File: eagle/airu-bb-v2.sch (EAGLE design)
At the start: 25 parts, among them Q2 MOSFET-NCHANNELAO3404A, U1 BMP180, U2 DHT22, U3 GPS, X2 53261-08

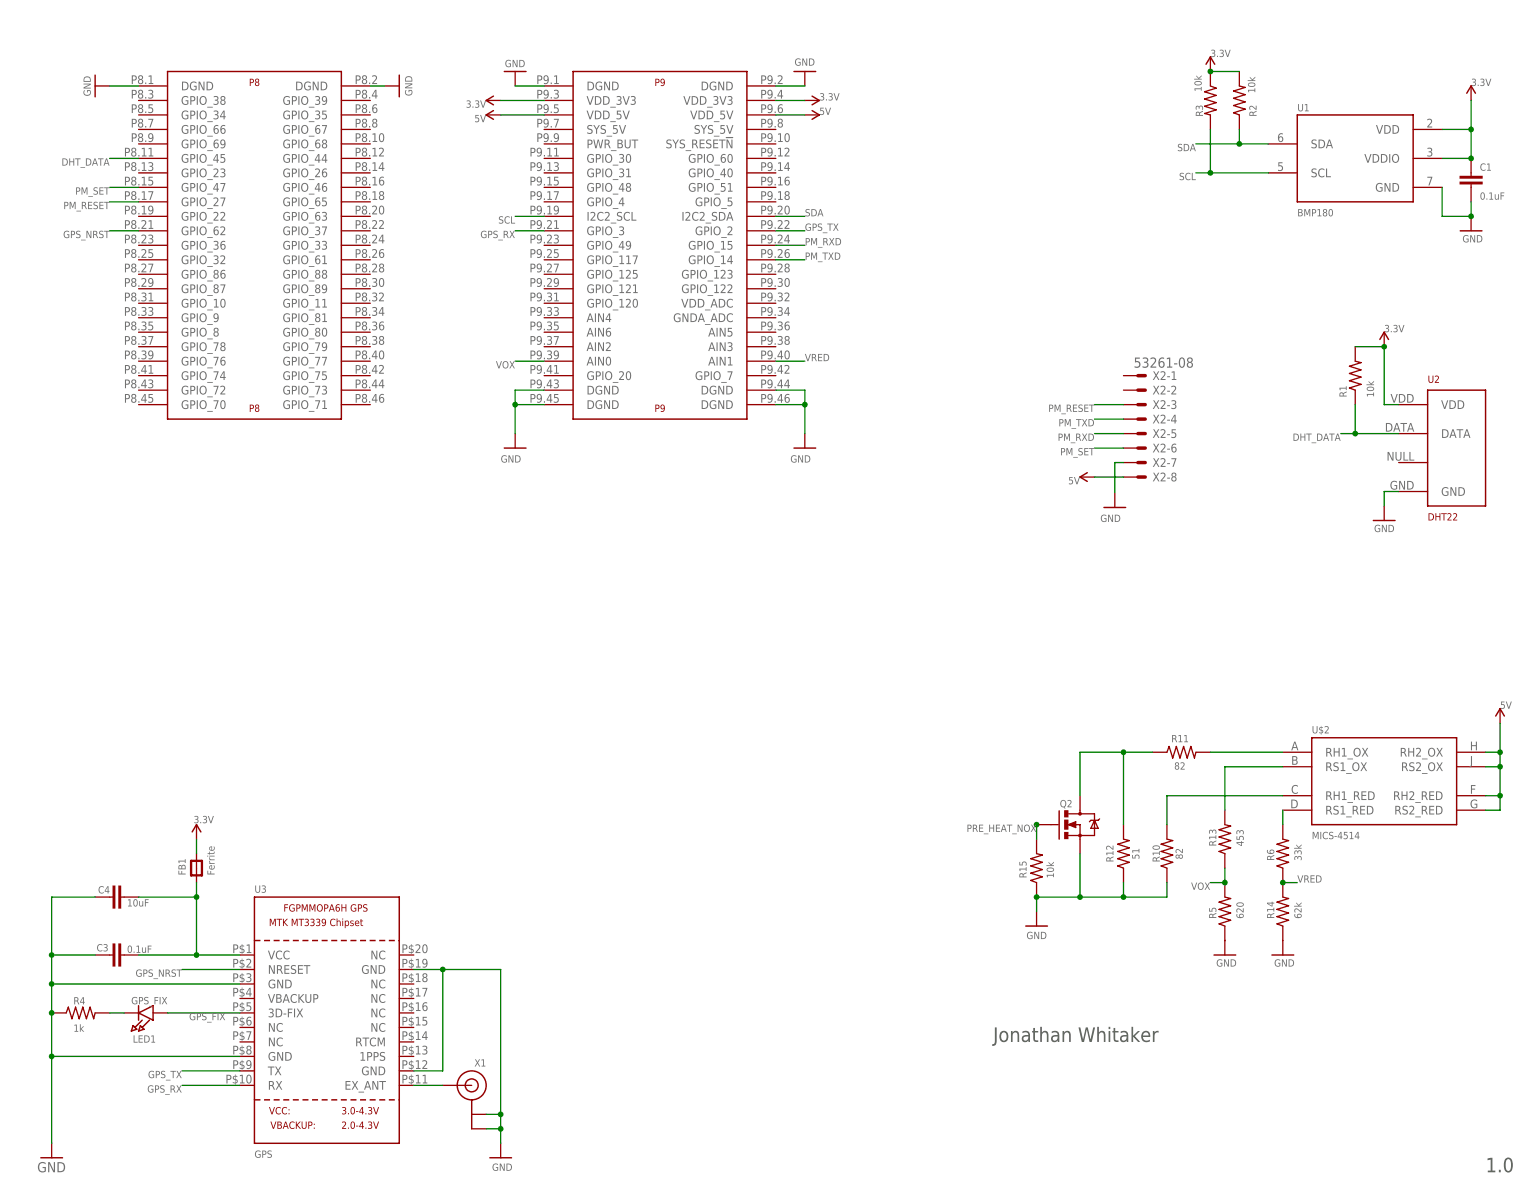
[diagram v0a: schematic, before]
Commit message: Added SPDT switch for operation mode and added RTC
This commit adds improvements to the schematic which includes a SPDT switch
that will be used to configure the operation mode of the station (lab/field use),
as well as a real-time clock so that time stamps can be used accurately offline.
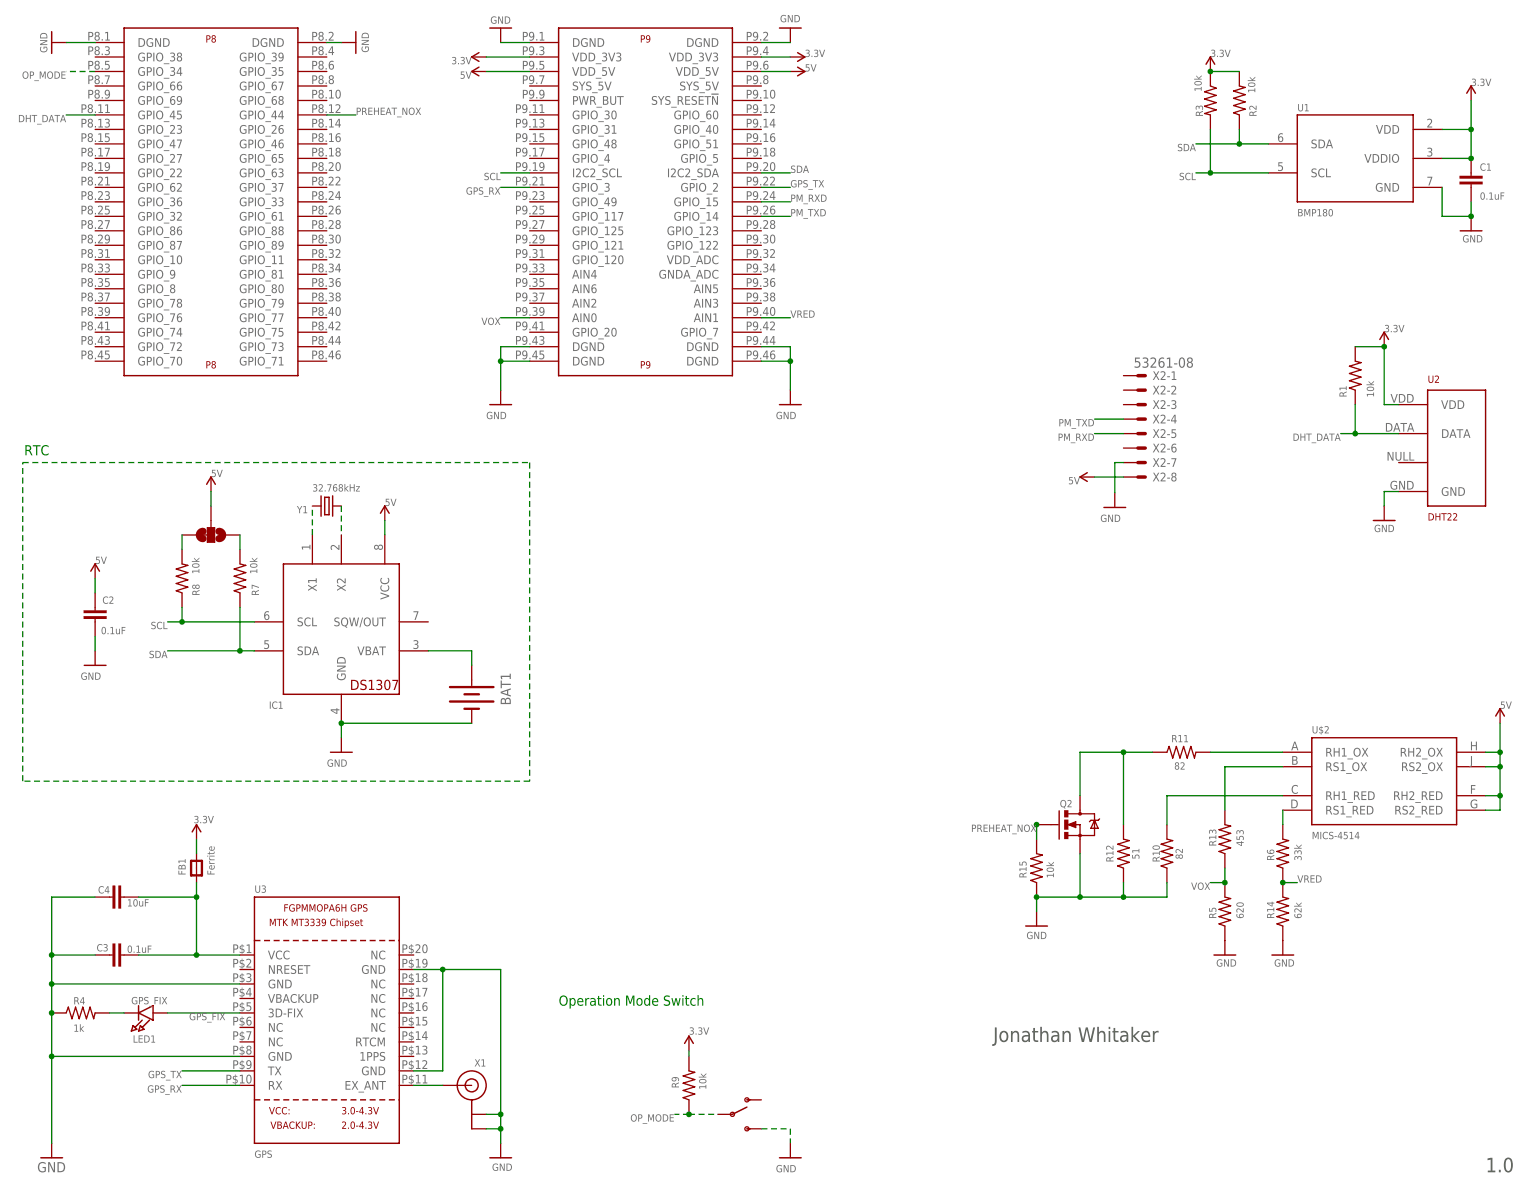
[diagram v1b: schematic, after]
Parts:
- added BAT1: (no value), SparkFun-Electromechanical:BATTERY20SMD
- added C2: 0.1uF, SparkFun-Passives:CAP1206
- added IC1: DS1307, adafruit:DS1307
- added R7, R8, R9: 10k, SparkFun-Passives:RESISTOR1206
- added SJ1: JUMPER-PAD-3-2OF3_NC_BY_TRACE_SMALL, SparkFun-Passives:JUMPER-PAD-3-2OF3_NC_BY_TRACE_SMALL
- added U$3: SWITCH_SPDT, SparkFun-Electromechanical:SWITCH_SPDT
- added Y1: 32.768kHz, SparkFun-FreqCtrl:CRYSTAL32-SMD
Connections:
- removed net GPS_NRST: U$1P8.GPIO_62, U3.NRESET
- removed net PM_RESET: U$1P8.GPIO_27, X2-3.S
- removed net PM_SET: U$1P8.GPIO_47, X2-6.S
- removed net PRE_HEAT_NOX: Q2.G, R15.2
- new net N$11: BAT1.+, IC1.VBAT
- new net N$12: IC1.X1, Y1.2
- new net N$13: R7.2, SJ1.1
- new net N$14: IC1.X2, Y1.1
- new net N$15: R8.2, SJ1.3
- new net OP_MODE: R9.1, U$1P8.GPIO_34, U$3.P
- new net PREHEAT_NOX: Q2.G, R15.2, U$1P8.GPIO_44
- net 3.3V: now also R9.2
- net 5V: now also C2.2, IC1.VCC, SJ1.2
- net GND: now also BAT1.-, C2.1, IC1.GND, U$3.S
- net SCL: now also IC1.SCL, R8.1
- net SDA: now also IC1.SDA, R7.1
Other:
- note added: "Operation Mode Switch"
- note added: "RTC"

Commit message: Added mode descriptions to the schematic
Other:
- note added: "Field Mode (1) / Lab Mode (0)"
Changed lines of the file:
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@@
 <text x="101.6" y="36.83" size="1.778" layer="91" font="vector">Operation Mode Switch</text>
 <wire x1="101.6" y1="35.56" x2="101.6" y2="5.08" width="0.1524" layer="98" style="longdash"/>
+<text x="104.14" y="7.62" size="0.8128" layer="91" font="vector">Field Mode (1) / Lab Mode (0)</text>
 </plain>
 <instances>
